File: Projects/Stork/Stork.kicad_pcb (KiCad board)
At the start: 4 copper layers, 200 x 100 mm, 559 parts, among them J25 Conn_02x03_Odd_Even, J26 Conn_01x03_Male, J27 Screw_Terminal_01x02, J28 Conn_01x03_Male, J29 Conn_01x03_Male, J30 Conn_01x03_Male, J31 Conn_02x05_Top_Bottom, J32 Conn_02x05_Top_Bottom, J33 Conn_02x05_Top_Bottom, J34 Conn_02x05_Top_Bottom, J35 Conn_02x05_Top_Bottom, J36 Conn_02x05_Top_Bottom, J37 Conn_02x05_Top_Bottom, J38 Conn_02x05_Top_Bottom, J39 Conn_02x05_Top_Bottom, J40 Conn_02x05_Top_Bottom, J41 Conn_02x05_Top_Bottom, J42 Conn_02x05_Top_Bottom, U1 AD7991YRJZ-1500RL7, U10 AD8608ARZ-SOIC127P600X175-14N, U11 AD7991YRJZ-1500RL7, U12 AD8608ARZ-SOIC127P600X175-14N, U13 AD7991YRJZ-1500RL7, U14 AD8608ARZ-SOIC127P600X175-14N, U15 AD7991YRJZ-1500RL7, U16 AD8608ARZ-SOIC127P600X175-14N, U17 AD7991YRJZ-1500RL7, U18 AD8608ARZ-SOIC127P600X175-14N, U19 AD7991YRJZ-1500RL7, U2 AD8608ARZ-SOIC127P600X175-14N, U20 AD8608ARZ-SOIC127P600X175-14N, U21 AD7991YRJZ-1500RL7, U22 AD8608ARZ-SOIC127P600X175-14N, U23 AD7991YRJZ-1500RL7, U24 AD8608ARZ-SOIC127P600X175-14N, U25 AD7991YRJZ-1500RL7, U26 AD8608ARZ-SOIC127P600X175-14N, U27 AD7991YRJZ-1500RL7, U28 AD8608ARZ-SOIC127P600X175-14N, U29 AD7991YRJZ-1500RL7, U3 AD7991YRJZ-1500RL7, U30 AD8608ARZ-SOIC127P600X175-14N, U31 AD7991YRJZ-1500RL7, U32 AD8608ARZ-SOIC127P600X175-14N, U33 Digilent-CoraZ7, U34 AD7991YRJZ-1500RL7, U35 AD8608ARZ-SOIC127P600X175-14N, U36 AD7991YRJZ-1500RL7, U37 AD8608ARZ-SOIC127P600X175-14N, U38 AD7991YRJZ-1500RL7, U39 AD8608ARZ-SOIC127P600X175-14N, U4 AD8608ARZ-SOIC127P600X175-14N, U40 AD7991YRJZ-1500RL7, U41 AD8608ARZ-SOIC127P600X175-14N, U42 AD7991YRJZ-1500RL7, U43 AD8608ARZ-SOIC127P600X175-14N, U44 AD7991YRJZ-1500RL7, U45 AD8608ARZ-SOIC127P600X175-14N, U46 AD7991YRJZ-1500RL7, U47 AD8608ARZ-SOIC127P600X175-14N, U48 AD7991YRJZ-1500RL7, U49 AD8608ARZ-SOIC127P600X175-14N, U5 AD7991YRJZ-1500RL7, U50 TPS79330-EP, U51 TPS73150DBV, U6 AD8608ARZ-SOIC127P600X175-14N, U7 AD7991YRJZ-1500RL7, U8 AD8608ARZ-SOIC127P600X175-14N, U9 AD7991YRJZ-1500RL7

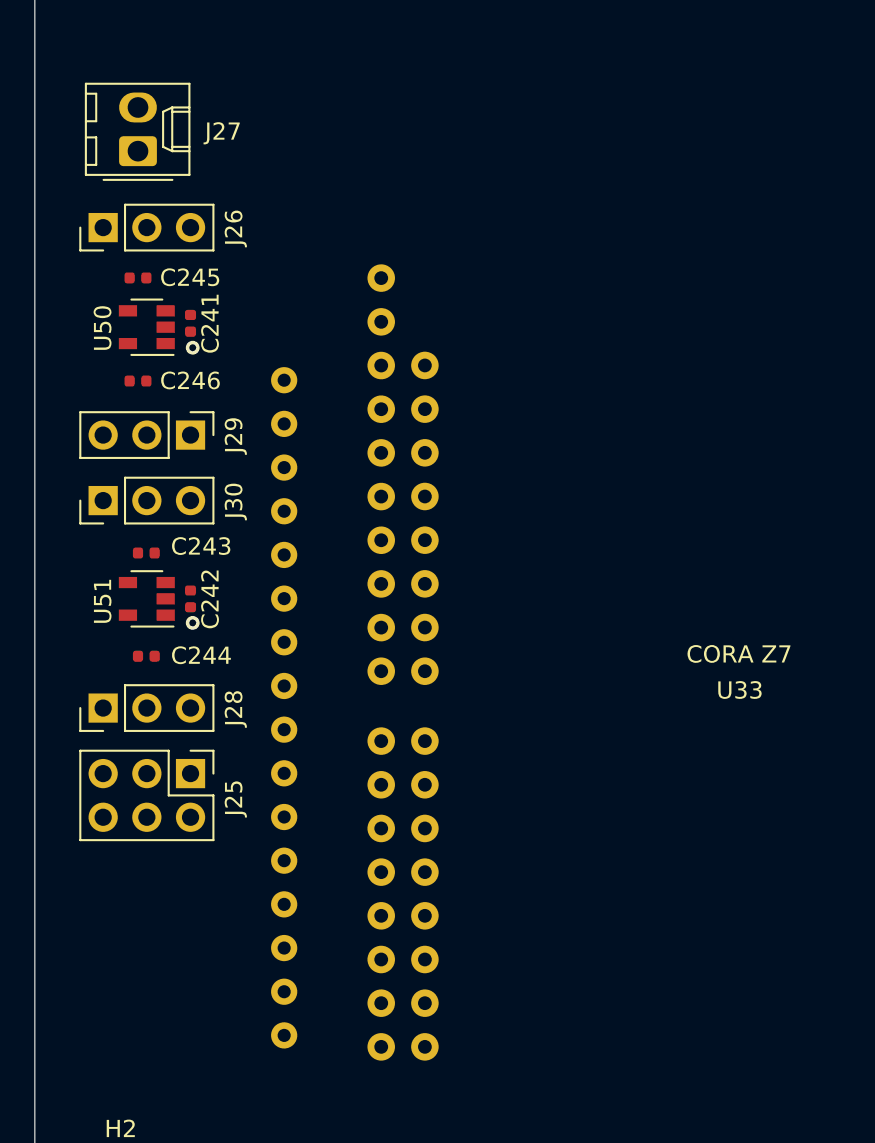
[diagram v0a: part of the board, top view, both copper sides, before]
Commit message: manually routed power section. library moved internally.
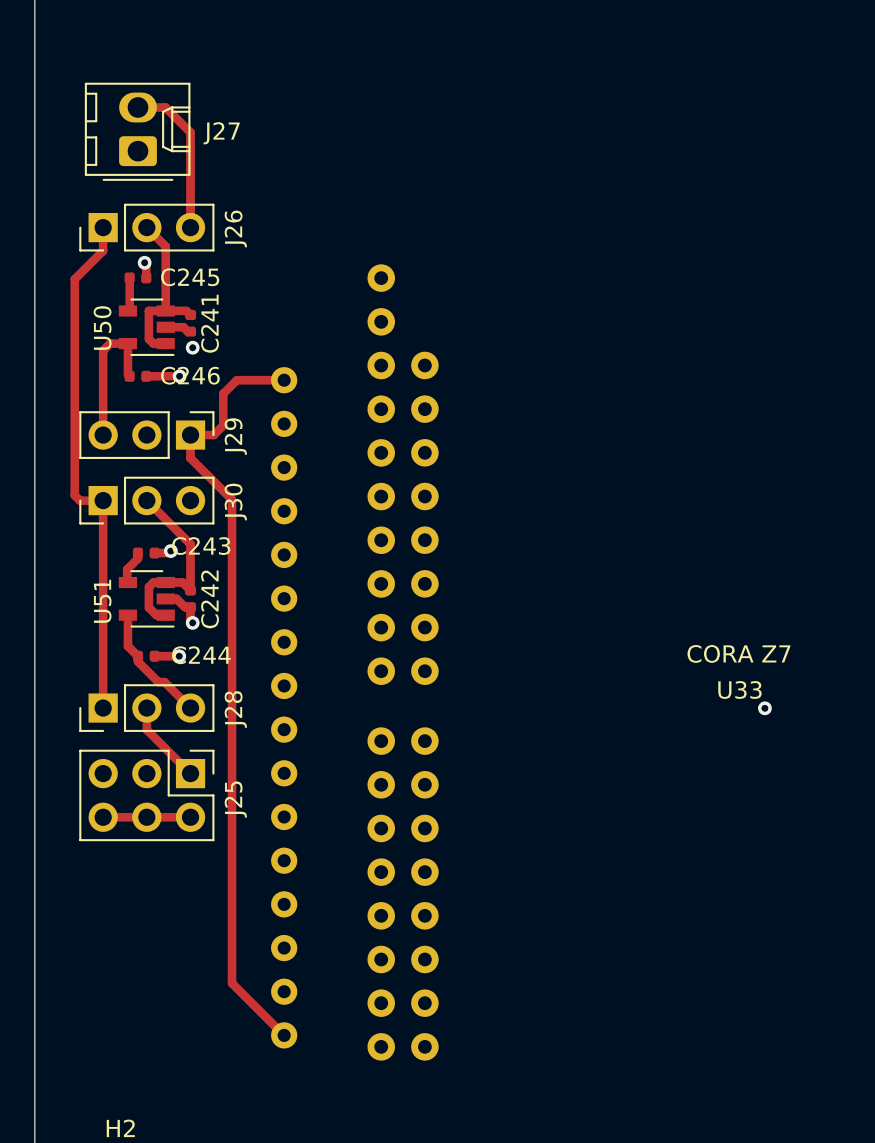
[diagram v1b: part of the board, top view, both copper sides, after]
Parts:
- moved C246 0.28 mm to (56.0, 77.7)
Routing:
- net 5V_CoraZ7: track 0.00 -> 99.5 mm, vias 0 -> 1
- net 3V3_CoraZ7: track 0.00 -> 45.0 mm
- net V_RAW: track 0.00 -> 29.6 mm
- net Net-(C242-Pad1): track 0.00 -> 11.4 mm
- net Net-(C241-Pad1): track 0.00 -> 10.5 mm
- net GND: track 0.00 -> 9.43 mm, vias 170 -> 174
- net 3V3_Reg: track 0.00 -> 8.47 mm
- net 5V_Reg: track 0.00 -> 7.12 mm
- net VDD_Filters: track 603.4 -> 608.5 mm
- net +5V: track 0.00 -> 4.86 mm
- net Net-(C243-Pad1): track 0.00 -> 1.99 mm
- net Net-(C245-Pad1): track 0.00 -> 1.96 mm
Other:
- net class Power removed

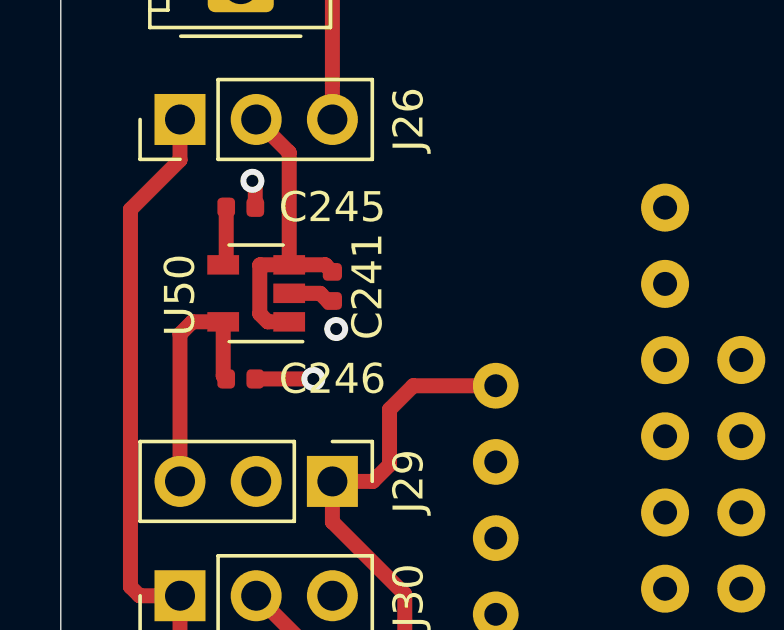
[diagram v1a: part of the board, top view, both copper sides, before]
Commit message: fixed via net near R229 and R235 to +3V3
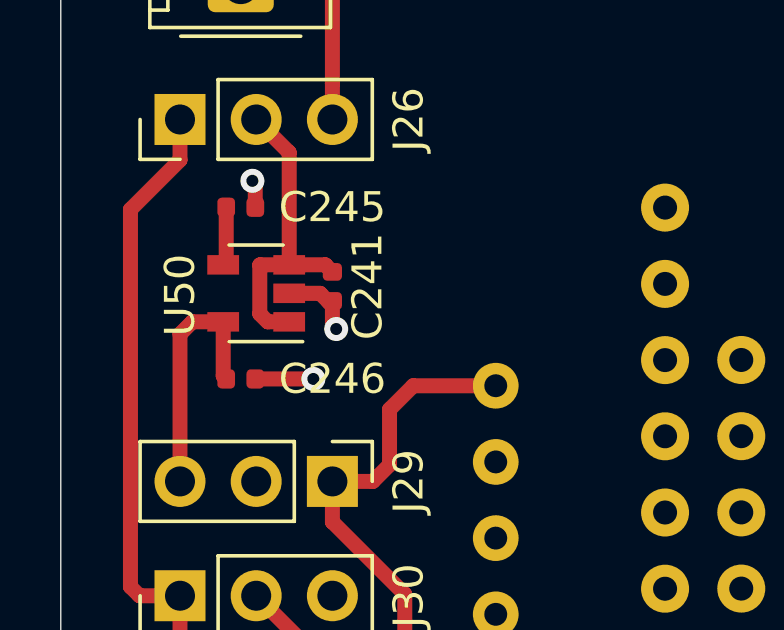
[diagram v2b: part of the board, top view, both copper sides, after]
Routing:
- net GND: track 9.43 -> 10.4 mm
- net SDA20: vias 1 -> 0
- net SCL7: vias 1 -> 0
- net SCL20: vias 1 -> 0
- net +3V3: vias 114 -> 117
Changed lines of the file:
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@@
     (thickness 1.6)
     (drawings 20)
-    (tracks 459)
+    (tracks 461)
     (zones 0)
     (modules 559)
@@
   (segment (start 58.900001 75.125) (end 59.055 75.125) (width 0.5) (layer F.Cu) (net 1))
   (segment (start 57.615 74.869999) (end 58.645 74.869999) (width 0.5) (layer F.Cu) (net 1))
+  (segment (start 59.055 75.933) (end 59.182 76.06) (width 0.5) (layer F.Cu) (net 1))
+  (segment (start 59.055 75.125) (end 59.055 75.933) (width 0.5) (layer F.Cu) (net 1))
   (via (at 127.508 85.09) (size 0.8) (drill 0.4) (layers F.Cu B.Cu) (net 382))
   (segment (start 56.515 98.285) (end 59.055 100.825) (width 0.5) (layer F.Cu) (net 383))
   (segment (start 56.515 97.015) (end 56.515 98.285) (width 0.5) (layer F.Cu) (net 383))
-  (via (at 127.508 106.68) (size 0.8) (drill 0.4) (layers F.Cu B.Cu) (net 405))
-  (via (at 122.936 107.95) (size 0.8) (drill 0.4) (layers F.Cu B.Cu) (net 422))
-  (via (at 122.936 110.49) (size 0.8) (drill 0.4) (layers F.Cu B.Cu) (net 428))
+  (via (at 127.508 106.68) (size 0.8) (drill 0.4) (layers F.Cu B.Cu) (net 436))
+  (via (at 122.936 107.95) (size 0.8) (drill 0.4) (layers F.Cu B.Cu) (net 436))
+  (via (at 122.936 110.49) (size 0.8) (drill 0.4) (layers F.Cu B.Cu) (net 436))
   (via (at 123 49.54) (size 0.8) (drill 0.4) (layers F.Cu B.Cu) (net 436))
   (via (at 123 47) (size 0.8) (drill 0.4) (layers F.Cu B.Cu) (net 436))

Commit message: routing complete
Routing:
- net GND: track 10.4 -> 232.7 mm
- net SDA5: track 0.00 -> 220.2 mm
- net SDA4: track 0.00 -> 195.6 mm
- net SCL5: track 0.00 -> 179.7 mm
- net SDA17: track 0.00 -> 179.4 mm, vias 0 -> 2
- net SCL11: track 0.00 -> 179.1 mm
- net SCL17: track 0.00 -> 178.0 mm, vias 0 -> 1
- net SDA11: track 0.00 -> 177.1 mm
- net SDA10: track 0.00 -> 170.5 mm
- net SCL4: track 0.00 -> 166.1 mm, vias 0 -> 1
- net SDA16: track 0.00 -> 161.9 mm, vias 0 -> 1
- net SCL16: track 0.00 -> 161.4 mm, vias 0 -> 1
- net SCL10: track 0.00 -> 157.8 mm
- net SCL15: track 0.00 -> 149.2 mm, vias 0 -> 1
- net +3V3: track 0.00 -> 138.6 mm
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
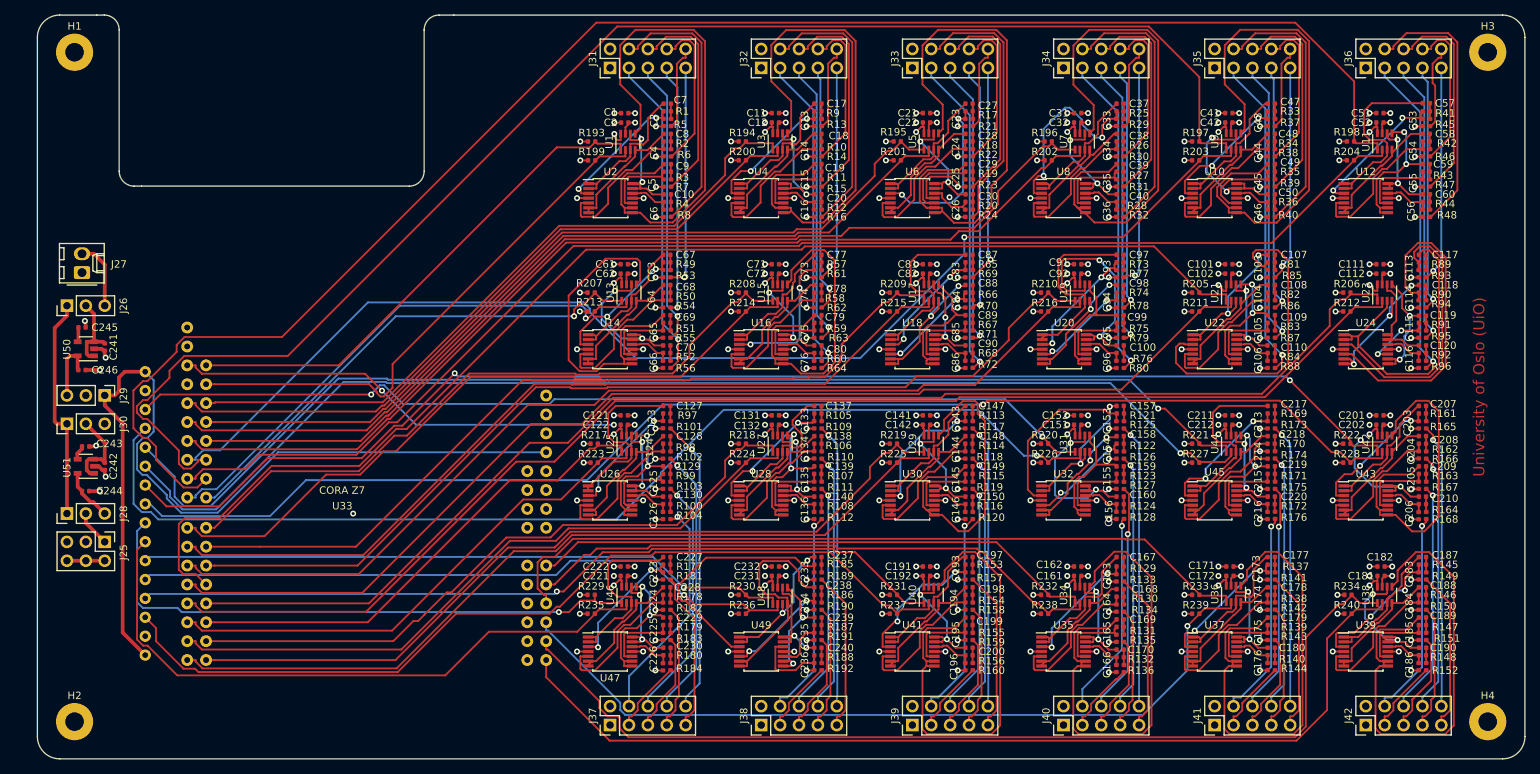
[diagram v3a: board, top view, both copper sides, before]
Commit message: updated copper pour on top and bottom layer
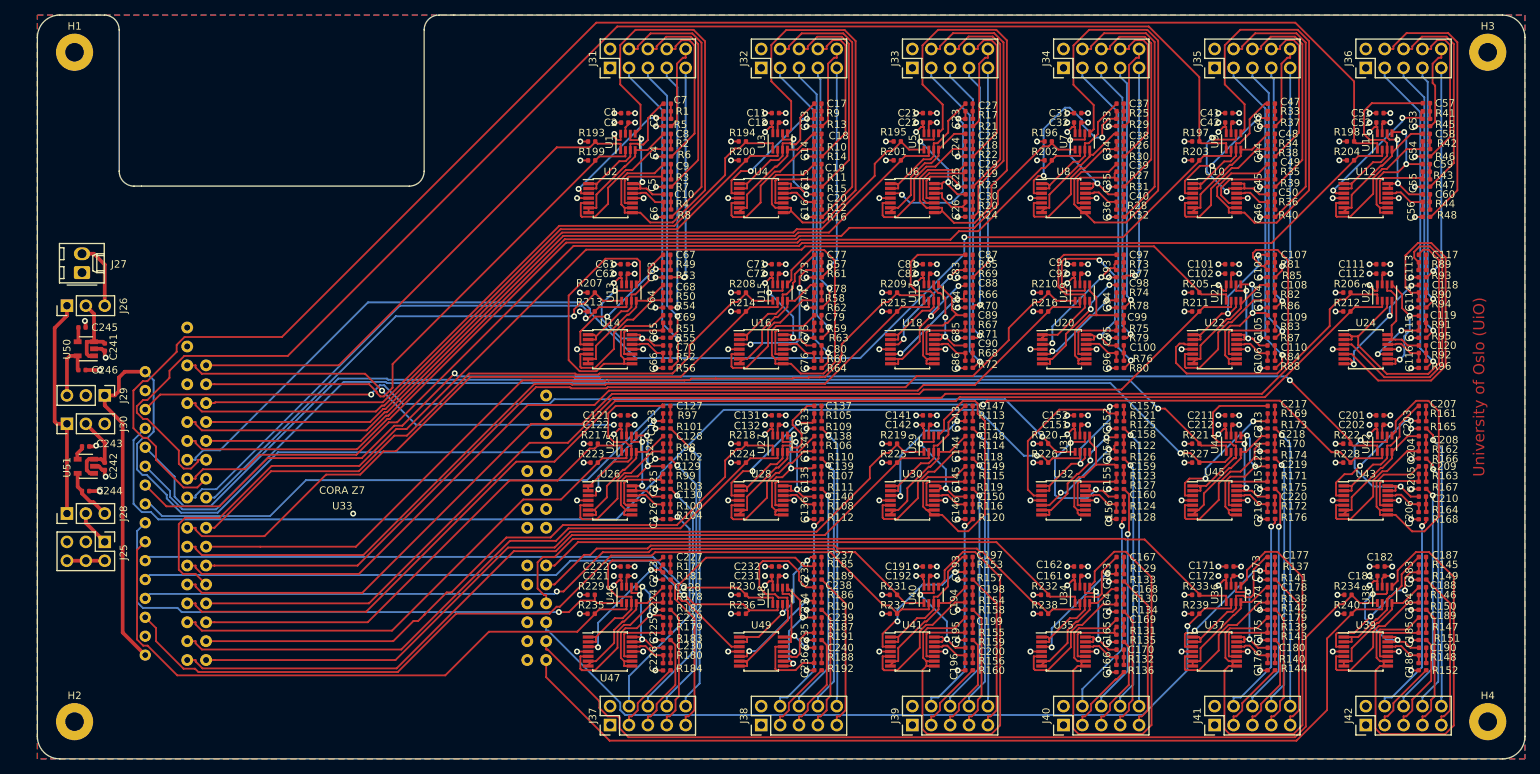
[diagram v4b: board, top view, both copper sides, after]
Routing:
- added copper zone on B.Cu, net GND
- added copper zone on F.Cu, net GND
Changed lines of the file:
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@@
+    )
+  )
+  (zone (net 1) (net_name GND) (layer F.Cu) (hatch edge 0.508)
+    (connect_pads (clearance 0.508))
+    (min_thickness 0.254)
+    (fill yes (arc_segments 32) (thermal_gap 0.508) (thermal_bridge_width 0.508))
+    (polygon
+      (pts
+        (xy 250 130) (xy 50 130) (xy 50 30) (xy 250 30)
+      )
+    )
+  )
+  (zone (net 1) (net_name GND) (layer B.Cu) (hatch edge 0.508)
+    (connect_pads (clearance 0.508))
+    (min_thickness 0.254)
+    (fill yes (arc_segments 32) (thermal_gap 0.508) (thermal_bridge_width 0.508))
+    (polygon
+      (pts
+        (xy 250 130) (xy 50 130) (xy 50 30) (xy 250 30)
+      )
     )
   )

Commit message: changed power pin to dc barrel jack
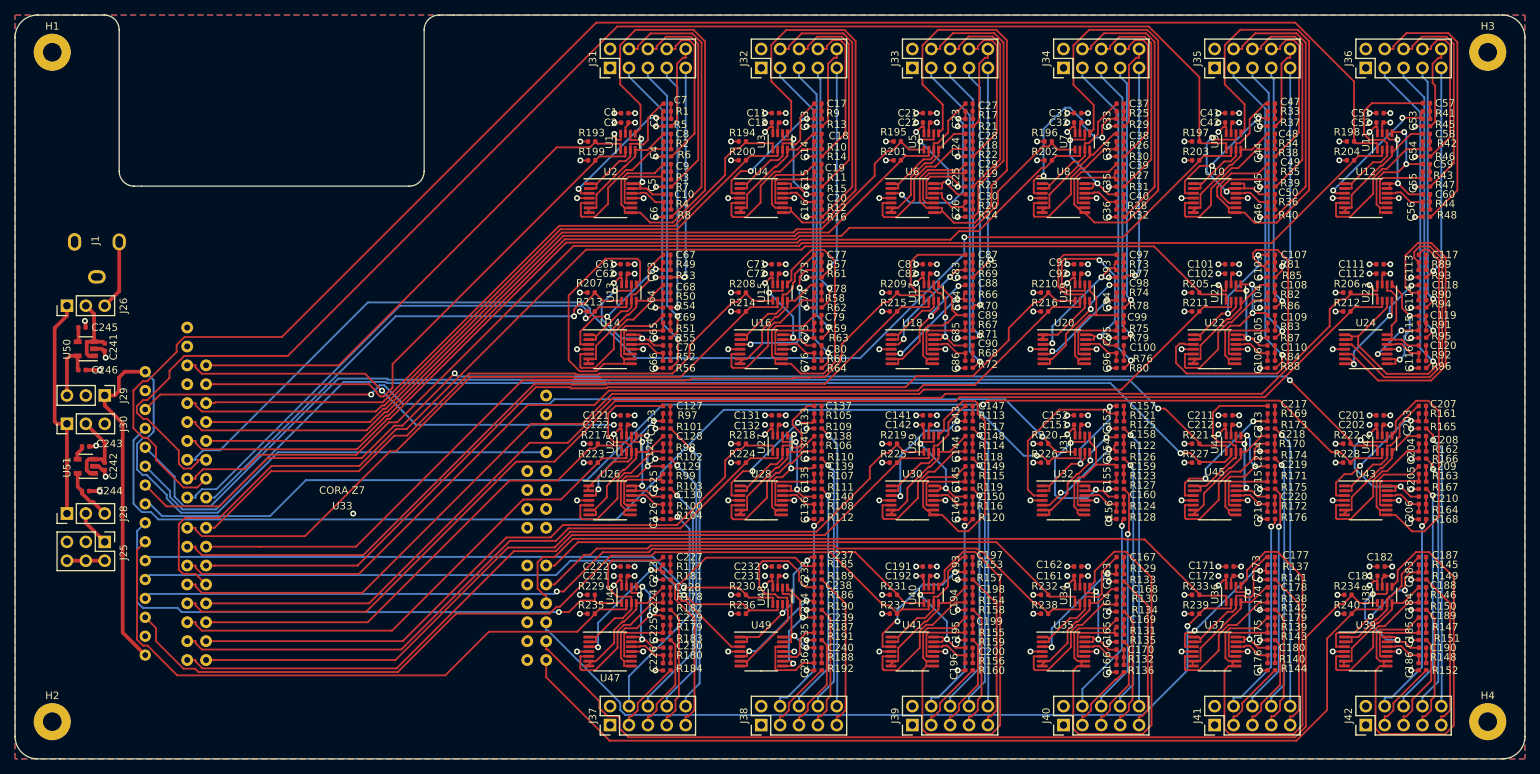
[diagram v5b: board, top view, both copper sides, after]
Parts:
- removed J27: Screw_Terminal_01x02, Connector_Molex:Molex_KK-254_AE-6410-02A_1x02_P2.54mm_Vertical
- added J1: Barrel_Jack_Switch, footprint:FC681465P, F.Cu at (58.0, 60.5)
- moved H1 3.00 mm to (52.0, 35.0)
- moved H2 3.00 mm to (52.0, 125.0)
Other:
- board size 200 x 100 mm -> 203 x 100 mm
- net class Default: clearance 0.2 -> 0.089; trace_width 0.25 -> 0.089
- rule trace_clearance: 0.2 -> 0.089
- rule trace_min: 0.2 -> 0.089
- board text removed: "University of Oslo (UiO)"

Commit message: added logo
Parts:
- added G***: LOGO, footprint:HPPSI_02_logo, F.Cu at (245.5, 104.7)
- added G***: LOGO, footprint:UiO_DoM, F.Cu at (245.3, 65.0)
